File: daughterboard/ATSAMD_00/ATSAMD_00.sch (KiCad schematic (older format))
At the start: 2 parts, among them J1 m2_keyA_67pin_daughterboard

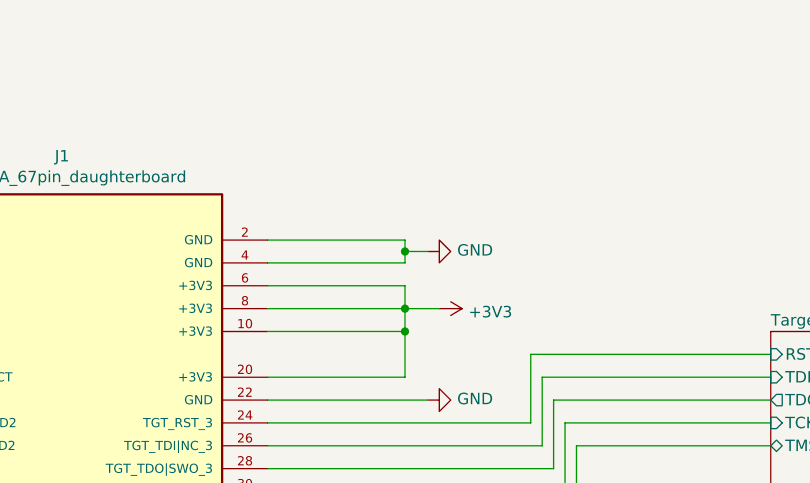
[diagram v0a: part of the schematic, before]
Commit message: ERC on daughterboards
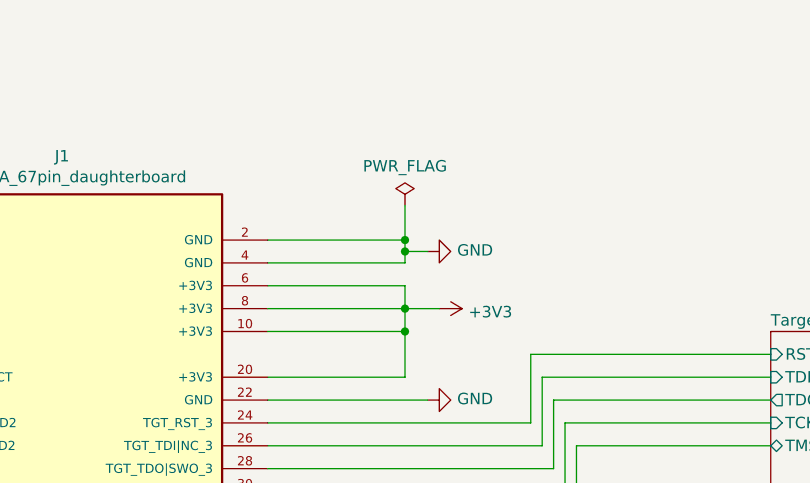
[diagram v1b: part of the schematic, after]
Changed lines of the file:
@@
 	0    -1   -1   0
 $EndComp
+$Comp
+L power:PWR_FLAG #FLG0101
+U 1 1 618F9EAB
+P 7500 1450
+F 0 "#FLG0101" H 7500 1525 50  0001 C CNN
+F 1 "PWR_FLAG" H 7500 1623 50  0000 C CNN
+F 2 "" H 7500 1450 50  0001 C CNN
+F 3 "~" H 7500 1450 50  0001 C CNN
+	1    7500 1450
+	1    0    0    -1
+$EndComp
+Wire Wire Line
+	7500 1600 7500 1450
+Connection ~ 7500 1600
 $EndSCHEMATC
